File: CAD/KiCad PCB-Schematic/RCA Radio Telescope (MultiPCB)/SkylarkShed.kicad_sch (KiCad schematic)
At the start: 6 parts

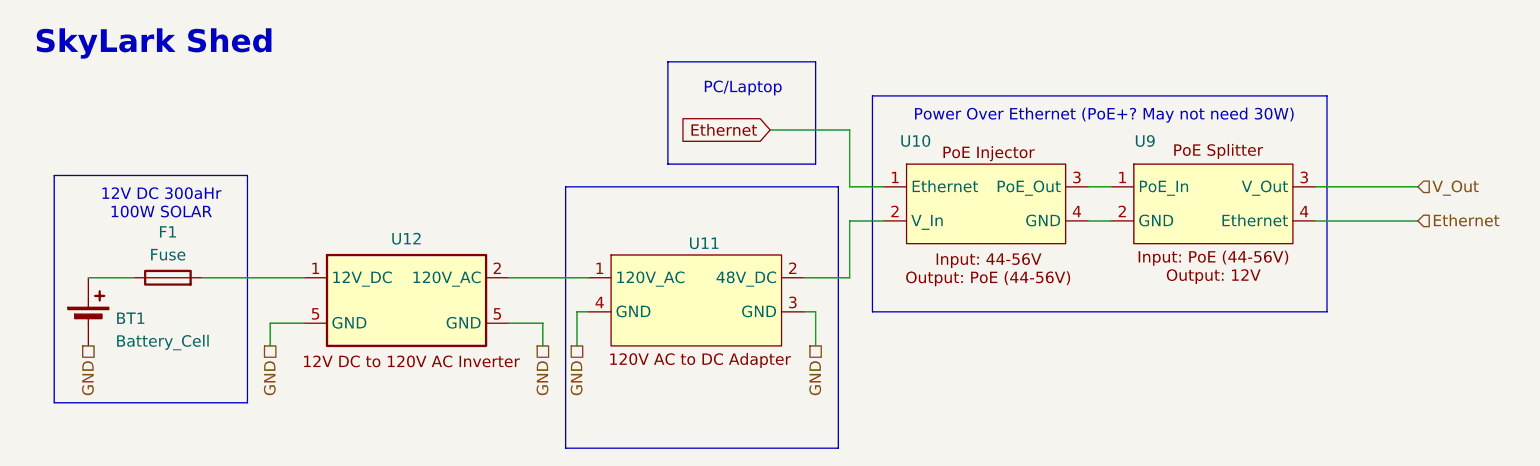
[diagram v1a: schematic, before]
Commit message: Updated Schematic to Fix USB/PMOS issues and Minor Fixes
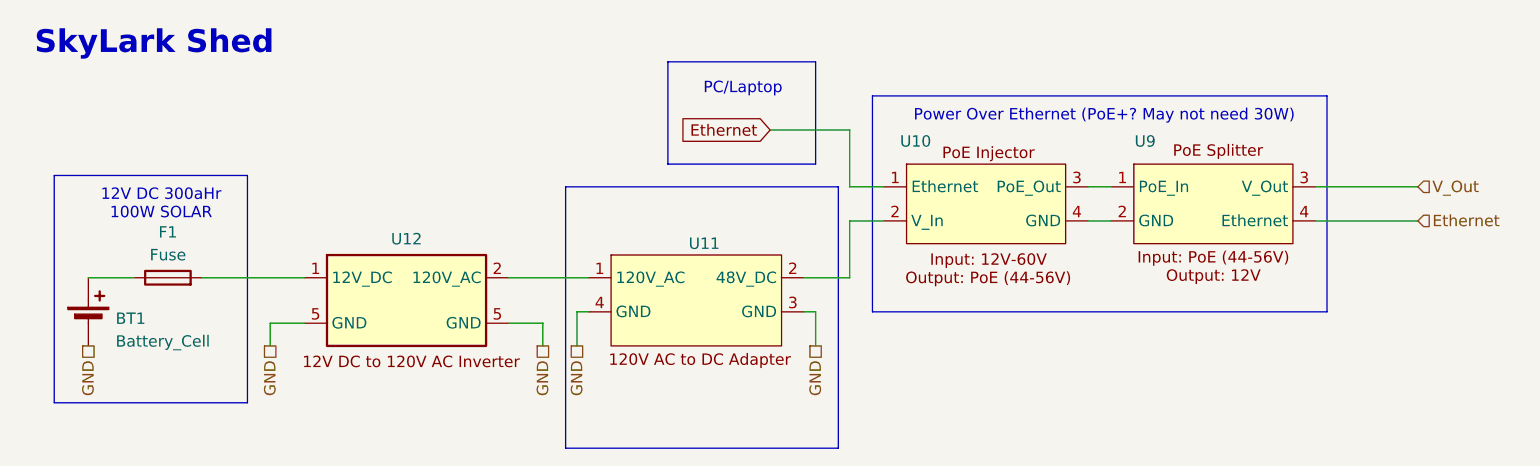
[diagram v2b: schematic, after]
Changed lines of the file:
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@@
 	(title_block
 		(title "Skylark Shed System")
-		(date "2025-03-30")
-		(rev "v1.0")
+		(date "2025-06-11")
+		(rev "v1.1")
 	)
 	(wire
@@
 		(shape passive)
 		(at 74.93 68.58 270)
-		(fields_autoplaced yes)
 		(effects
 			(font
@@
 		(shape passive)
 		(at 105.41 68.58 270)
-		(fields_autoplaced yes)
 		(effects
 			(font
@@
 		(shape passive)
 		(at 44.45 68.58 270)
-		(fields_autoplaced yes)
 		(effects
 			(font
@@
 		(shape passive)
 		(at 78.74 68.58 270)
-		(fields_autoplaced yes)
 		(effects
 			(font
@@
 		(shape input)
 		(at 172.72 54.61 0)
-		(fields_autoplaced yes)
 		(effects
 			(font
@@
 		(shape passive)
 		(at 24.13 68.58 270)
-		(fields_autoplaced yes)
 		(effects
 			(font
@@
 		(shape input)
 		(at 172.72 50.8 0)
-		(fields_autoplaced yes)
-		(effects
-			(font
+		(effects
+			(font
